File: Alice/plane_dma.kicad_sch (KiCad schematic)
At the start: 42 parts, among them Q647 NOT_OC, Q648 NOT_OC, Q649 NOT_OC, Q650 NOT_OC, Q651 NOT_OC, Q652 NOT_OC, Q653 NOT_OC, Q654 NOT_OC, Q655 NOT_OC, Q656 NOT_OC, Q657 NOT_OC, Q658 NOT_OC, Q659 NOT_OC, Q660 NOT_OC, Q661 NOT_OC, Q662 NOT_OC

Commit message: DMA bitplane sheet updated
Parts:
- added AND_94, AND_95, AND_96, AND_97, AND_98: AND2, symbol NMOS:AND2
- added BPRUN_SR1, BPSTOP_SR1, BPSTOP_SR2, HCE_SR1, VW_SR1: SR, symbol NMOS:SR
- added BP_TR1, BP_TR2, BP_TR3, BP_TR4: TR, symbol NMOS:TR
- added BUF_3, BUF_4: BUF, symbol NMOS:BUF
- added DWC_CMP0, DWC_CMP1, DWC_CMP10, DWC_CMP11, DWC_CMP2, DWC_CMP3, DWC_CMP4, DWC_CMP5, DWC_CMP6, DWC_CMP7, DWC_CMP8, DWC_CMP9, DWS_CMP0, DWS_CMP1, DWS_CMP10, DWS_CMP2, DWS_CMP3, DWS_CMP4, DWS_CMP5, DWS_CMP6, DWS_CMP7, DWS_CMP8, DWS_CMP9: CMPD, symbol NMOS:CMPD
- added MUX21, MUX22: MUX, symbol NMOS:MUX
- added NAND_6: NAND3, symbol NMOS:NAND3
- added NAND_7: NAND2, symbol NMOS:NAND2
- added NOR_28: NOR3, symbol NMOS:NOR3
- added NOT_31, NOT_32: NOT, symbol NMOS:NOT
- added OR_30, OR_31: OR2, symbol NMOS:OR2
- added Q663, Q664, Q665, Q666, Q667, Q668, Q669, Q670, Q671, Q672, Q673, Q674, Q675, Q676: NOT_OC, symbol NMOS:NOT_OC
- added R80, R81, R82, R83: PULLUP, symbol NMOS:PULLUP
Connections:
- net BMAPEN: now also AND_91.5, NAND_6.2; no longer AND_91.3
- net BPE: now also AND_91.3; no longer AND_91.5
- net HARDDIS: now also NOR_28.2
- net HCTR1: now also BUF_4.2
- net LEW: now also BPRUN_SR1.7 (S)
- net NHCTR1: now also BUF_3.2
- net PHI1: now also BPRUN_SR1.4 (C1), BPSTOP_SR1.4 (C1), BPSTOP_SR2.4 (C1), BP_TR1.4 (C1), BP_TR2.4 (C1), BP_TR3.4 (C1), BP_TR4.4 (C1), DWC_CMP0.4 (C1), DWC_CMP1.4 (C1), DWC_CMP10.4 (C1), DWC_CMP11.4 (C1), DWC_CMP2.4 (C1), DWC_CMP3.4 (C1), DWC_CMP4.4 (C1), DWC_CMP5.4 (C1), DWC_CMP6.4 (C1), DWC_CMP7.4 (C1), DWC_CMP8.4 (C1), DWC_CMP9.4 (C1), DWS_CMP0.4 (C1), DWS_CMP1.4 (C1), DWS_CMP10.4 (C1), DWS_CMP2.4 (C1), DWS_CMP3.4 (C1), DWS_CMP4.4 (C1), DWS_CMP5.4 (C1), DWS_CMP6.4 (C1), DWS_CMP7.4 (C1), DWS_CMP8.4 (C1), DWS_CMP9.4 (C1), HCE_SR1.4 (C1), VW_SR1.4 (C1)
- net PHI2: now also BPRUN_SR1.5 (C2), BPSTOP_SR1.5 (C2), BPSTOP_SR2.5 (C2), BP_TR1.5 (C2), BP_TR2.5 (C2), BP_TR3.5 (C2), BP_TR4.5 (C2), HCE_SR1.5 (C2), VW_SR1.5 (C2)
- net TEW: now also AND_96.2
- net VARBEAMEN: now also NOR_28.3
- net VCC: now also DWC_CMP0.5 (EQI), DWS_CMP0.5 (EQI), R80.1 (S), R81.1 (S), R82.1 (S), R83.1 (S); no longer AND_91.4
- new net: DWS_CMP4.6 (EQO), DWS_CMP5.5 (EQI)
- new net: DWS_CMP5.6 (EQO), DWS_CMP6.5 (EQI)
- new net: BP_TR1.3 (R), BP_TR2.3 (R), BP_TR3.3 (R), BP_TR4.3 (R), NOT_32.1
- new net: AND_94.2, DWC_CMP11.2 (VV), NOT_31.1
- new net: DWC_CMP11.5 (EQI), DWC_CMP7.6 (EQO), DWC_CMP8.5 (EQI)
- new net: DWC_CMP11.6 (EQO), MUX22.4 (D0)
- new net: DWC_CMP0.6 (EQO), DWC_CMP1.5 (EQI)
- new net: DWS_CMP1.6 (EQO), DWS_CMP2.5 (EQI)
- new net: DWS_CMP2.6 (EQO), DWS_CMP3.5 (EQI)
- new net: HCE_SR1.6 (R), OR_30.1
- new net: BPRUN_SR1.6 (R), NAND_6.1
- new net: DWC_CMP1.6 (EQO), DWC_CMP2.5 (EQI)
- new net: DWS_CMP8.6 (EQO), DWS_CMP9.5 (EQI)
- new net: DWS_CMP10.5 (EQI), DWS_CMP9.6 (EQO)
- new net: AND_94.1, MUX21.4 (D0)
- new net: AND_94.3, DWS_CMP7.6 (EQO), DWS_CMP8.5 (EQI)
- new net: DWS_CMP3.6 (EQO), DWS_CMP4.5 (EQI)
- new net: DWC_CMP4.6 (EQO), DWC_CMP5.5 (EQI)
- new net: DWC_CMP5.6 (EQO), DWC_CMP6.5 (EQI)
- new net: DWS_CMP10.6 (EQO), MUX21.3 (D1)
- new net: DWC_CMP2.6 (EQO), DWC_CMP3.5 (EQI)
- new net: DWS_CMP0.6 (EQO), DWS_CMP1.5 (EQI)
- new net: DWS_CMP6.6 (EQO), DWS_CMP7.5 (EQI)
- new net: DWC_CMP8.6 (EQO), DWC_CMP9.5 (EQI)
- new net: DWC_CMP6.6 (EQO), DWC_CMP7.5 (EQI)
- new net: OR_31.1, VW_SR1.6 (R)
- new net: AND_95.1, OR_31.2
- new net: AND_95.3, NOR_28.1
- new net: DWC_CMP10.5 (EQI), DWC_CMP9.6 (EQO)
- new net: DWC_CMP10.6 (EQO), MUX22.3 (D1)
- new net: AND_98.1, BPSTOP_SR2.6 (R)
- new net: DWC_CMP3.6 (EQO), DWC_CMP4.5 (EQI)
- new net BPLAST: NAND_6.4, NAND_7.1
- new net BPN15: BP_TR4.6 (T), Q665.1, Q669.1, Q672.1, Q674.1, R82.3 (D)
- new net BPN3: BP_TR2.6 (T), Q663.1, Q667.1, R80.3 (D)
- new net BPN31: Q666.1, Q670.1, Q673.1, Q675.1, Q676.1, R83.3 (D)
- new net BPN7: BP_TR3.6 (T), Q664.1, Q668.1, Q671.1, R81.3 (D)
- new net BPRUN: AND_96.3, BPRUN_SR1.1 (Q), NOT_32.2
- new net BPS0: BP_TR1.6 (T), BUF_4.1
- new net BPS1: BP_TR1.1 (Q)
- new net BPS2: BP_TR2.1 (Q)
- new net BPS3: BP_TR3.1 (Q)
- new net BPS4: BP_TR4.1 (Q)
- new net BPSTOP: AND_98.3, BPSTOP_SR1.6 (R), BPSTOP_SR2.1 (Q), NAND_7.2
- new net BPSTOPREQ: AND_97.2, BPSTOP_SR1.1 (Q)
- new net BPVSTART: MUX21.1 (S), VW_SR1.7 (S)
- new net BPVSTOP: MUX22.1 (S), OR_31.3
- new net BSVB: AND_95.2
- new net DB10: DWC_CMP10.1 (DB), DWC_CMP2.1 (DB), DWS_CMP10.1 (DB), DWS_CMP2.1 (DB)
- new net DB11: DWC_CMP3.1 (DB), DWS_CMP3.1 (DB)
- new net DB12: DWC_CMP4.1 (DB), DWS_CMP4.1 (DB)
- new net DB13: DWC_CMP5.1 (DB), DWS_CMP5.1 (DB)
- new net DB14: DWC_CMP6.1 (DB), DWS_CMP6.1 (DB)
- new net DB15: DWC_CMP11.1 (DB), DWC_CMP7.1 (DB), DWS_CMP7.1 (DB)
- new net DB8: DWC_CMP0.1 (DB), DWC_CMP8.1 (DB), DWS_CMP0.1 (DB), DWS_CMP8.1 (DB)
- new net DB9: DWC_CMP1.1 (DB), DWC_CMP9.1 (DB), DWS_CMP1.1 (DB), DWS_CMP9.1 (DB)
- new net DIWHIGH: DWC_CMP10.3 (LD), DWC_CMP8.3 (LD), DWC_CMP9.3 (LD), DWS_CMP10.3 (LD), DWS_CMP8.3 (LD), DWS_CMP9.3 (LD), HCE_SR1.7 (S)
- new net DIWSTOP: DWC_CMP0.3 (LD), DWC_CMP1.3 (LD), DWC_CMP11.3 (LD), DWC_CMP2.3 (LD), DWC_CMP3.3 (LD), DWC_CMP4.3 (LD), DWC_CMP5.3 (LD), DWC_CMP6.3 (LD), DWC_CMP7.3 (LD), OR_30.3
- new net DIWSTRT: DWS_CMP0.3 (LD), DWS_CMP1.3 (LD), DWS_CMP2.3 (LD), DWS_CMP3.3 (LD), DWS_CMP4.3 (LD), DWS_CMP5.3 (LD), DWS_CMP6.3 (LD), DWS_CMP7.3 (LD), OR_30.2
- new net HCE: HCE_SR1.1 (Q), MUX21.2 (SEL), MUX22.2 (SEL)
- new net LAST: AND_97.3, AND_98.2, NAND_7.3
- new net NBPS0: BUF_3.1, Q663.2, Q664.2, Q665.2, Q666.2
- new net NBPS1: BP_TR1.2 (~{Q}), Q667.2, Q668.2, Q669.2, Q670.2
- new net NBPS2: BP_TR2.2 (~{Q}), Q671.2, Q672.2, Q673.2
- new net NBPS3: BP_TR3.2 (~{Q}), Q674.2, Q675.2
- new net NBPS4: BP_TR4.2 (~{Q}), Q676.2
- new net REQS: AND_96.1, BPSTOP_SR1.7 (S)
- new net STOPS: AND_97.1, BPSTOP_SR2.7 (S)
- new net VARVBEN: NOR_28.4
- new net VCTR0: DWC_CMP0.2 (VV), DWS_CMP0.2 (VV)
- new net VCTR1: DWC_CMP1.2 (VV), DWS_CMP1.2 (VV)
- new net VCTR10: DWC_CMP10.2 (VV), DWS_CMP10.2 (VV)
- new net VCTR2: DWC_CMP2.2 (VV), DWS_CMP2.2 (VV)
- new net VCTR3: DWC_CMP3.2 (VV), DWS_CMP3.2 (VV)
- new net VCTR4: DWC_CMP4.2 (VV), DWS_CMP4.2 (VV)
- new net VCTR5: DWC_CMP5.2 (VV), DWS_CMP5.2 (VV)
- new net VCTR6: DWC_CMP6.2 (VV), DWS_CMP6.2 (VV)
- new net VCTR7: DWC_CMP7.2 (VV), DWS_CMP7.2 (VV)
- new net VCTR8: DWC_CMP8.2 (VV), DWS_CMP8.2 (VV), NOT_31.2
- new net VCTR9: DWC_CMP9.2 (VV), DWS_CMP9.2 (VV)
- new net VW: AND_91.4, NAND_6.3, VW_SR1.1 (Q)
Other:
- note added: "Display Data Fetch comparators"
- note added: "Display Vertical Window comparators"
- moved on the sheet: BPE_SR1, DFC_CMP2, DFC_CMP3, DFC_CMP4, DFC_CMP5, DFC_CMP6, DFC_CMP7, DFC_CMP8, DFS_CMP2, DFS_CMP3, DFS_CMP4, DFS_CMP5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

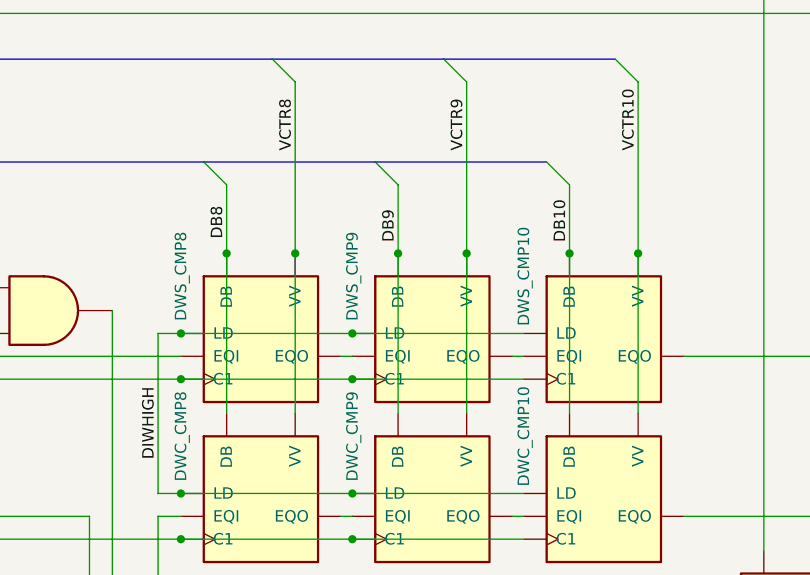
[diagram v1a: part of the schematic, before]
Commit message: BPLCON0 and FMODE registers added
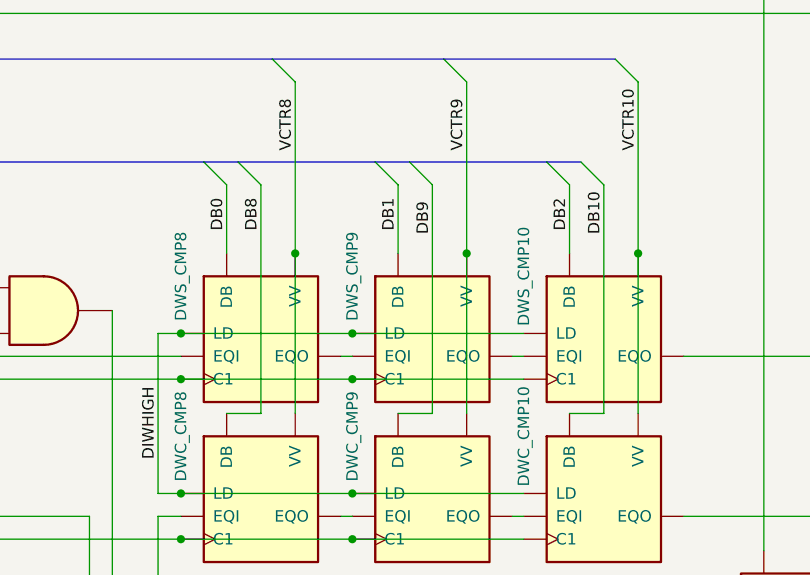
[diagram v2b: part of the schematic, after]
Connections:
- net DB1: now also DWS_CMP9.1 (DB)
- net DB10: no longer DWS_CMP10.1 (DB)
- net DB2: now also DWS_CMP10.1 (DB)
- net DB8: no longer DWS_CMP8.1 (DB)
- net DB9: no longer DWS_CMP9.1 (DB)
- new net DB0: DWS_CMP8.1 (DB)
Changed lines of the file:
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@@
   (junction (at 402.59 130.81) (diameter 0) (color 0 0 0 0)
   )
-  (junction (at 238.76 124.46) (diameter 0) (color 0 0 0 0)
-  )
   (junction (at 90.17 43.18) (diameter 0) (color 0 0 0 0)
   )
@@
   )
   (junction (at 96.52 138.43) (diameter 0) (color 0 0 0 0)
-  )
-  (junction (at 257.81 124.46) (diameter 0) (color 0 0 0 0)
-  )
-  (junction (at 276.86 124.46) (diameter 0) (color 0 0 0 0)
   )
   (junction (at 128.27 43.18) (diameter 0) (color 0 0 0 0)
@@
     (stroke (width 0) (type default) (color 0 0 0 0))
   )
+  (bus_entry (at 240.03 114.3) (size 2.54 2.54)
+    (stroke (width 0) (type default) (color 0 0 0 0))
+  )
+  (bus_entry (at 278.13 114.3) (size 2.54 2.54)
+    (stroke (width 0) (type default) (color 0 0 0 0))
+  )
+  (bus_entry (at 259.08 114.3) (size 2.54 2.54)
+    (stroke (width 0) (type default) (color 0 0 0 0))
+  )
   (bus_entry (at 80.01 50.8) (size 2.54 2.54)
     (stroke (width 0) (type default) (color 0 0 0 0))
@@
     (stroke (width 0) (type default) (color 0 0 0 0))
   )
-  (wire (pts (xy 276.86 124.46) (xy 276.86 142.24))
-    (stroke (width 0) (type default) (color 0 0 0 0))
-  )
   (wire (pts (xy 233.68 41.91) (xy 233.68 45.72))
     (stroke (width 0) (type default) (color 0 0 0 0))
@@
     (stroke (width 0) (type default) (color 0 0 0 0))
   )
+  (wire (pts (xy 280.67 142.24) (xy 276.86 142.24))
+    (stroke (width 0) (type default) (color 0 0 0 0))
+  )
   (wire (pts (xy 34.29 153.67) (xy 39.37 153.67))
     (stroke (width 0) (type default) (color 0 0 0 0))
@@
     (stroke (width 0) (type default) (color 0 0 0 0))
   )
-  (wire (pts (xy 257.81 124.46) (xy 257.81 142.24))
-    (stroke (width 0) (type default) (color 0 0 0 0))
-  )
   (wire (pts (xy 193.04 92.71) (xy 320.04 92.71))
     (stroke (width 0) (type default) (color 0 0 0 0))
   )
+  (wire (pts (xy 261.62 142.24) (xy 257.81 142.24))
+    (stroke (width 0) (type default) (color 0 0 0 0))
+  )
   (wire (pts (xy 339.09 71.12) (xy 339.09 74.93))
     (stroke (width 0) (type default) (color 0 0 0 0))
@@
     (stroke (width 0) (type default) (color 0 0 0 0))
   )
-  (bus (pts (xy 236.22 114.3) (xy 255.27 114.3))
+  (bus (pts (xy 236.22 114.3) (xy 240.03 114.3))
     (stroke (width 0) (type default) (color 0 0 0 0))
   )
@@
     (stroke (width 0) (type default) (color 0 0 0 0))
   )
+  (wire (pts (xy 280.67 116.84) (xy 280.67 142.24))
+    (stroke (width 0) (type default) (color 0 0 0 0))
+  )
   (wire (pts (xy 120.65 58.42) (xy 120.65 76.2))
     (stroke (width 0) (type default) (color 0 0 0 0))
@@
     (stroke (width 0) (type default) (color 0 0 0 0))
   )
+  (bus (pts (xy 240.03 114.3) (xy 255.27 114.3))
+    (stroke (width 0) (type default) (color 0 0 0 0))
+  )
   (wire (pts (xy 101.6 124.46) (xy 101.6 142.24))
     (stroke (width 0) (type default) (color 0 0 0 0))
@@
     (stroke (width 0) (type default) (color 0 0 0 0))
   )
-  (wire (pts (xy 238.76 124.46) (xy 238.76 142.24))
-    (stroke (width 0) (type default) (color 0 0 0 0))
-  )
   (wire (pts (xy 293.37 55.88) (xy 289.56 55.88))
     (stroke (width 0) (type default) (color 0 0 0 0))
@@
     (stroke (width 0) (type default) (color 0 0 0 0))
   )
+  (wire (pts (xy 261.62 116.84) (xy 261.62 142.24))
+    (stroke (width 0) (type default) (color 0 0 0 0))
+  )
   (wire (pts (xy 402.59 125.73) (xy 424.18 125.73))
     (stroke (width 0) (type default) (color 0 0 0 0))
@@
     (stroke (width 0) (type default) (color 0 0 0 0))
   )
+  (wire (pts (xy 242.57 116.84) (xy 242.57 142.24))
+    (stroke (width 0) (type default) (color 0 0 0 0))
+  )
   (wire (pts (xy 421.64 92.71) (xy 393.7 92.71))
     (stroke (width 0) (type default) (color 0 0 0 0))
@@
     (stroke (width 0) (type default) (color 0 0 0 0))
   )
+  (bus (pts (xy 274.32 114.3) (xy 278.13 114.3))
+    (stroke (width 0) (type default) (color 0 0 0 0))
+  )
   (wire (pts (xy 109.22 58.42) (xy 109.22 76.2))
     (stroke (width 0) (type default) (color 0 0 0 0))
@@
     (stroke (width 0) (type default) (color 0 0 0 0))
   )
+  (wire (pts (xy 238.76 142.24) (xy 242.57 142.24))
+    (stroke (width 0) (type default) (color 0 0 0 0))
+  )
   (wire (pts (xy 171.45 135.89) (xy 172.72 135.89))
     (stroke (width 0) (type default) (color 0 0 0 0))
@@
     (stroke (width 0) (type default) (color 0 0 0 0))
   )
-  (bus (pts (xy 255.27 114.3) (xy 274.32 114.3))
+  (bus (pts (xy 255.27 114.3) (xy 259.08 114.3))
     (stroke (width 0) (type default) (color 0 0 0 0))
   )
@@
   )
   (wire (pts (xy 58.42 67.31) (xy 77.47 67.31))
+    (stroke (width 0) (type default) (color 0 0 0 0))
+  )
+  (bus (pts (xy 259.08 114.3) (xy 274.32 114.3))
     (stroke (width 0) (type default) (color 0 0 0 0))
   )
@@
     (effects (font (size 1.27 1.27)) (justify left bottom))
   )
+  (label "DB10" (at 280.67 122.3047 90)
+    (effects (font (size 1.27 1.27)) (justify left bottom))
+  )
   (label "VW" (at 294.64 71.12 0)
     (effects (font (size 1.27 1.27)) (justify left bottom))
@@
     (effects (font (size 1.27 1.27)) (justify left bottom))
   )
-  (label "DB9" (at 257.81 123.19 90)
+  (label "DB1" (at 257.81 121.92 90)
     (effects (font (size 1.27 1.27)) (justify left bottom))
   )
@@
   )
   (label "NHCTR2" (at 173.99 36.83 90)
+    (effects (font (size 1.27 1.27)) (justify left bottom))
+  )
+  (label "DB9" (at 261.62 122.3047 90)
     (effects (font (size 1.27 1.27)) (justify left bottom))
   )
@@
     (effects (font (size 1.27 1.27)) (justify left bottom))
   )
-  (label "DB10" (at 276.86 123.19 90)
+  (label "DB2" (at 276.86 121.92 90)
     (effects (font (size 1.27 1.27)) (justify left bottom))
   )
@@
     (effects (font (size 1.27 1.27)) (justify left bottom))
   )
-  (label "DB8" (at 238.76 122.8053 90)
+  (label "DB0" (at 238.76 121.92 90)
     (effects (font (size 1.27 1.27)) (justify left bottom))
   )
@@
     (effects (font (size 1.27 1.27)) (justify left bottom))
   )
+  (label "DB8" (at 242.57 121.92 90)
+    (effects (font (size 1.27 1.27)) (justify left bottom))
+  )

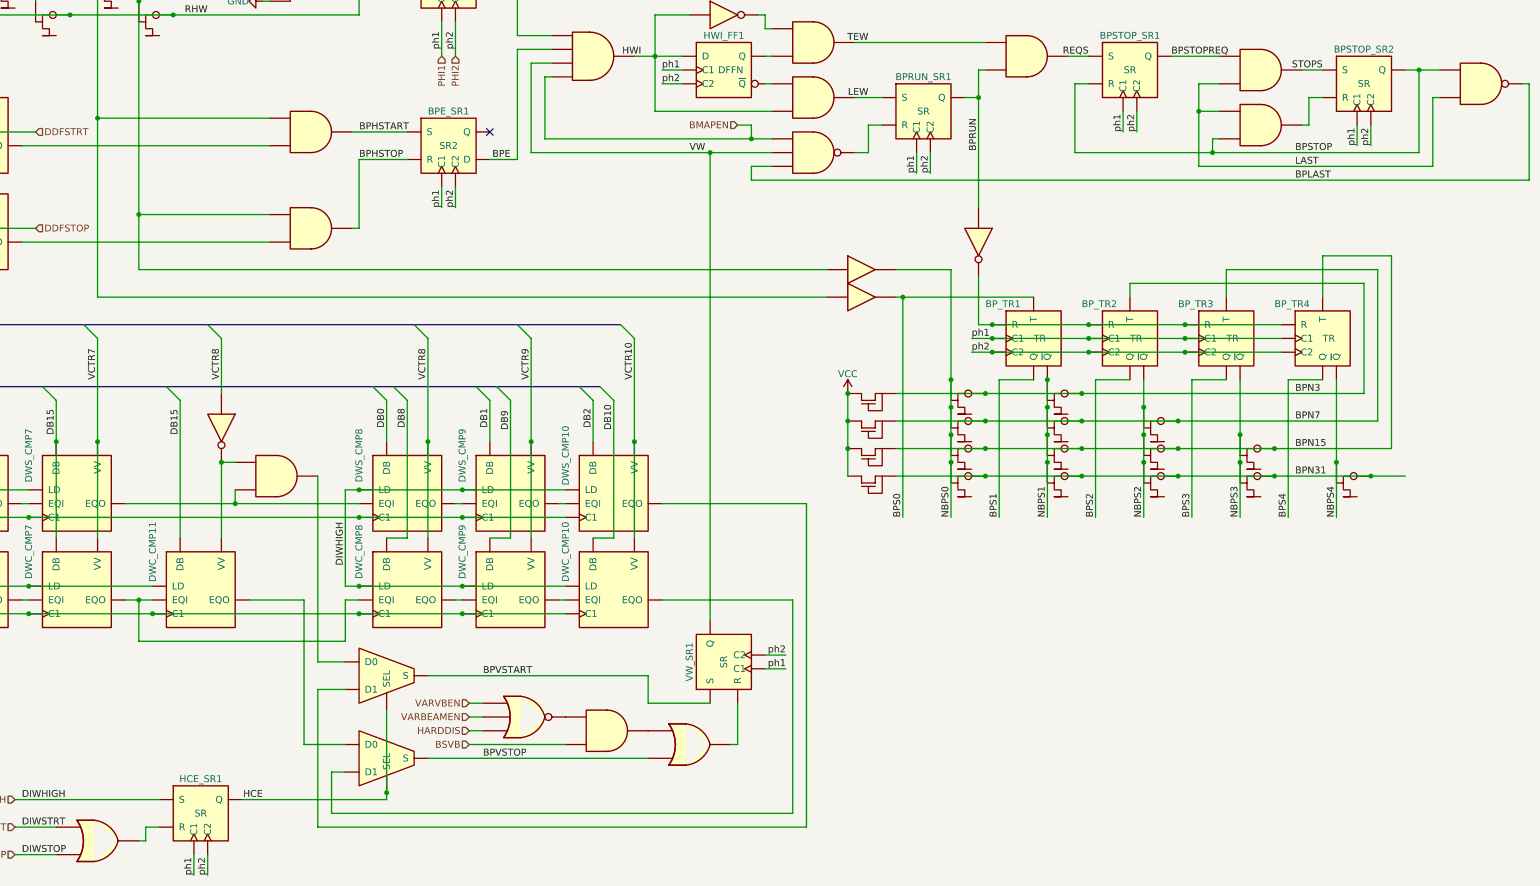
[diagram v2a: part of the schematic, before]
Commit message: Started adding BPCYC16 and BPCYC32 logic for AGA fetch modes
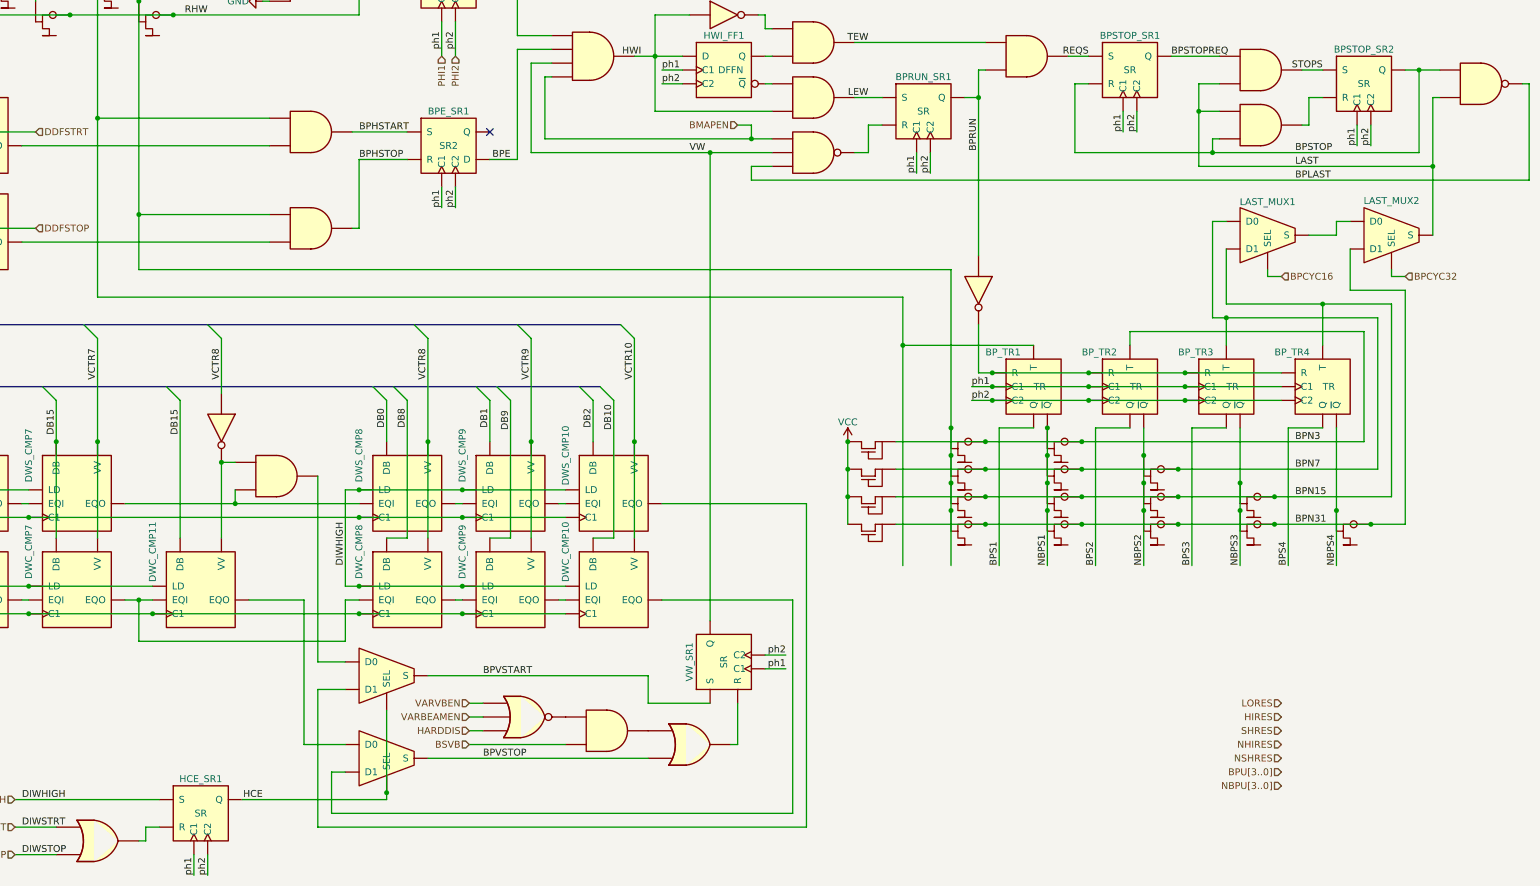
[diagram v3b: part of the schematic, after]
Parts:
- removed BUF_3, BUF_4: BUF, symbol NMOS:BUF
- added LAST_MUX1, LAST_MUX2: MUX, symbol NMOS:MUX
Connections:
- net BPS0 is gone; now on net HCTR1: BP_TR1.6 (T)
- net NBPS0 is gone; now on net NHCTR1: Q663.2, Q664.2, Q665.2, Q666.2
- net BPN15: now also LAST_MUX1.3 (D1)
- net BPN31: now also LAST_MUX2.3 (D1)
- net BPN7: now also LAST_MUX1.4 (D0)
- net LAST: now also LAST_MUX2.1 (S)
- new net: LAST_MUX1.1 (S), LAST_MUX2.4 (D0)
- new net BPCYC16: LAST_MUX1.2 (SEL)
- new net BPCYC32: LAST_MUX2.2 (SEL)
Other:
- moved on the sheet: BP_TR1, BP_TR2, BP_TR3, BP_TR4
